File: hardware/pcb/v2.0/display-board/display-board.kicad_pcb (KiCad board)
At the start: 4 copper layers, 92 x 30 mm, 59 parts, among them J1 Conn_01x01_Socket, J2 Conn_01x01_Socket, J3 Conn_01x01_Socket, J4 Conn_01x01_Socket, J5 Conn_01x01_Socket, J6 Conn_01x01_Socket, Q1 AO3400A, Q2 AO3401A, Q3 AO3400A, Q4 AO3401A, Q5 AO3400A, Q6 AO3401A, Q7 AO3400A, SW1 SW_Push, SW2 SW_Push, U1 TLC5940PWP, U2 7Seg 2Dig 0.56in, U3 GS-S2011AB, U4 7Seg 2Dig 0.56in, U5 GS-S2011AB

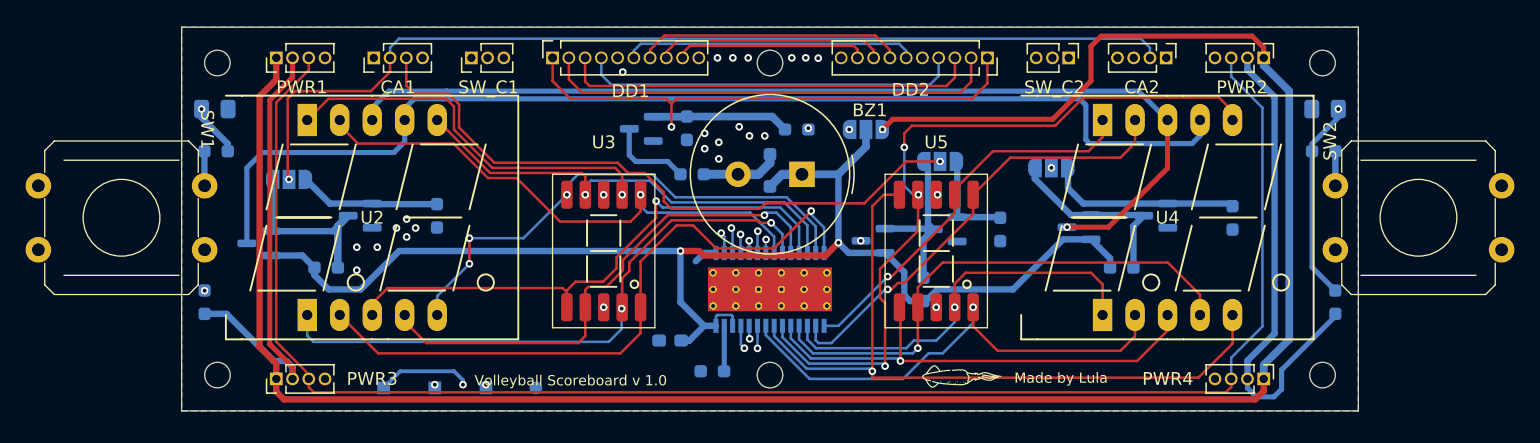
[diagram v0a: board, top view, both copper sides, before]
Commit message: v2.0 of the main and display board is ready and in production
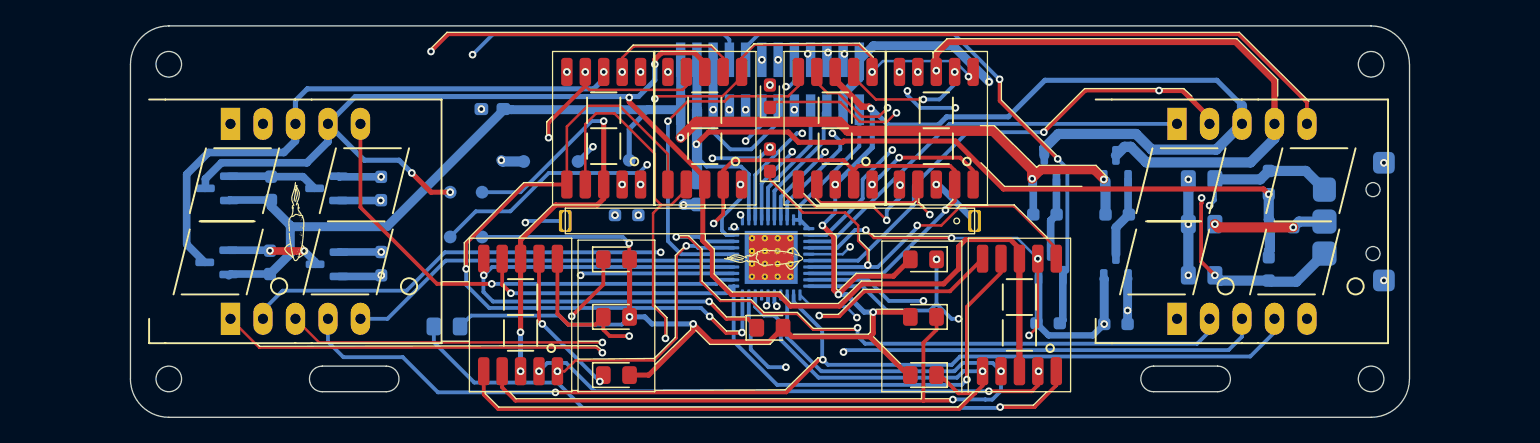
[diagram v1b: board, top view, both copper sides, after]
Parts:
- removed BAT+, CTRL: TestPoint_Pad_1.0x1.0mm, TestPoint:TestPoint_Pad_1.0x1.0mm
- removed BZ1: Buzzer, Buzzer_Beeper:Buzzer_TDK_PS1240P02BT_D12.2mm_H6.5mm
- removed CA1, CA2, PWR1, PWR2, PWR3, PWR4: Conn_01x04_Pin, Connector_PinHeader_1.27mm:PinHeader_1x04_P1.27mm_Vertical
- removed DD1, DD2: Conn_01x10_Pin, Connector_PinSocket_1.27mm:PinSocket_1x10_P1.27mm_Vertical
- removed J1, J2, J3, J4, J5, J6: Conn_01x01_Socket, MountingHole:MountingHole_2mm
- removed the LDO at (73.8, 110.7)
- removed PWRQ1, PWRQ2, PWRQ3, PWR_S1: SolderJumper_3_Open, Jumper:SolderJumper-3_P1.3mm_Open_RoundedPad1.0x1.5mm_NumberLabels
- removed the R10 at (102.1, 90.5)
- removed R13: 1k, Resistor_SMD:R_0603_1608Metric_Pad0.98x0.95mm_HandSolder
- removed the R8 at (93.9, 94.0)
- removed the R9 at (93.5, 90.4)
- removed SW2: SW_Push, Luis:Button_12x12x7.3
- removed SW_C1, SW_C2: Conn_01x03_Pin, Connector_PinHeader_1.27mm:PinHeader_1x03_P1.27mm_Vertical
- removed U1: TLC5940PWP, Package_SO:HTSSOP-28-1EP_4.4x9.7mm_P0.65mm_EP3.4x9.5mm_Mask2.4x6.17mm_ThermalVias
- added 1: TestPoint, TestPoint:TestPoint_Pad_D1.0mm, B.Cu at (77.5, 95.4)
- added 2: TestPoint, TestPoint:TestPoint_Pad_D1.0mm, B.Cu at (75.0, 95.4)
- added 3: TestPoint, TestPoint:TestPoint_Pad_D1.0mm, B.Cu at (77.5, 98.9)
- added 4: TestPoint, TestPoint:TestPoint_Pad_D1.0mm, B.Cu at (75.0, 98.9)
- added A1: Conn_02x12_Odd_Even, Connector_PinHeader_1.27mm:PinHeader_2x12_P1.27mm_Vertical_SMD, B.Cu at (100.0, 87.0)
- added C2: 0.1uF, Capacitor_SMD:C_0603_1608Metric_Pad1.08x0.95mm_HandSolder, B.Cu at (94.3, 95.5)
- added C5: 2.2uF, Capacitor_SMD:C_0805_2012Metric_Pad1.18x1.45mm_HandSolder, B.Cu at (133.7, 94.4)
- added D10: LED, LED_SMD:LED_0603_1608Metric_Pad1.05x0.95mm_HandSolder, F.Cu at (100.0, 87.9)
- added D11: LED, LED_SMD:LED_0603_1608Metric_Pad1.05x0.95mm_HandSolder, F.Cu at (100.0, 92.9)
- added D3: LED, LED_SMD:LED_0805_2012Metric_Pad1.15x1.40mm_HandSolder, F.Cu at (88.0, 100.7)
- added D4: LED, LED_SMD:LED_0805_2012Metric_Pad1.15x1.40mm_HandSolder, F.Cu at (88.0, 105.2)
- added D5: LED, LED_SMD:LED_0805_2012Metric_Pad1.15x1.40mm_HandSolder, F.Cu at (88.0, 109.7)
- added D6: LED, LED_SMD:LED_0805_2012Metric_Pad1.15x1.40mm_HandSolder, F.Cu at (100.0, 106.0)
- added D7: LED, LED_SMD:LED_0805_2012Metric_Pad1.15x1.40mm_HandSolder, F.Cu at (112.0, 100.7)
- added D8: LED, LED_SMD:LED_0805_2012Metric_Pad1.15x1.40mm_HandSolder, F.Cu at (112.0, 105.2)
- added D9: LED, LED_SMD:LED_0805_2012Metric_Pad1.15x1.40mm_HandSolder, F.Cu at (112.0, 109.7)
- added DTEST: LED, LED_SMD:LED_0805_2012Metric_Pad1.15x1.40mm_HandSolder, B.Cu at (74.7, 105.9)
- added G***: LOGO, Luis:lula1, F.Cu at (99.5, 100.6)
- added G***: LOGO, Luis:lula1, F.Cu at (62.9, 97.7)
- added G***: LOGO, Luis:lula1, B.Cu at (140.0, 109.9)
- added H1: MountingHole, MountingHole:MountingHole_2mm, F.Cu at (53.0, 85.4)
- added H2: MountingHole, MountingHole:MountingHole_2mm, F.Cu at (147.0, 85.4)
- added H3: MountingHole, MountingHole:MountingHole_2mm, F.Cu at (53.0, 110.0)
- added H4: MountingHole, MountingHole:MountingHole_2mm, F.Cu at (147.0, 110.0)
- added LDO: TestPoint, TestPoint:TestPoint_Pad_D1.0mm, B.Cu at (85.0, 93.0)
- added Q8: AO3401A, Package_TO_SOT_SMD:SOT-23, B.Cu at (127.0, 93.5)
- added R1: 651, Resistor_SMD:R_0603_1608Metric_Pad0.98x0.95mm_HandSolder, B.Cu at (88.8, 97.2)
- added R12: 10K, Resistor_SMD:R_0603_1608Metric_Pad0.98x0.95mm_HandSolder, B.Cu at (127.1, 97.2)
- added TCL5951: TLC5951RHA, Package_DFN_QFN:Texas_RHA0040B_VQFN-40-1EP_6x6mm_P0.5mm_EP4.15x4.15mm_ThermalVias, B.Cu at (100.1, 100.5)
- added U2: GS-S2011AB, Luis:GS-2011AB, F.Cu at (87.0, 90.4)
- added U5: GS-S2011AB, Luis:GS-2011AB, F.Cu at (94.9, 90.4)
- added U7: GS-S2011AB, Luis:GS-2011AB, F.Cu at (105.1, 90.4)
- added U9: GS-S2011AB, Luis:GS-2011AB, F.Cu at (113.0, 90.4)
- added VCC: TestPoint, TestPoint:TestPoint_Pad_D1.0mm, B.Cu at (89.0, 92.9)
- C1: value C -> 10uF
- C3: renamed from C2; value 0.1uF -> 2.2uF
- C4: renamed from C3; value 0.1uF -> 2.2uF
- D1: value D -> LED; footprint Diode_SMD:D_SOD-323_HandSoldering -> Luis:LED Bar; moved to F.Cu
- G***: moved to B.Cu
- GND: value TestPoint_Pad_D1.0mm -> TestPoint
- R11: value 1k -> 10K
- R4: value 651 -> 100k
- SW1: value SW_Push -> ~; footprint Luis:Button_12x12x7.3 -> Luis:Thumbwheel; moved to B.Cu
- moved SW1 97.8 mm to (147.1, 97.7), turned to 90 degrees
- moved R3 84.4 mm to (140.0, 98.2), turned to 0 degrees
- moved C4 77.7 mm to (133.7, 97.9), turned to 180 degrees
- moved Q4 67.4 mm to (56.8, 95.1)
- moved R8 66.8 mm to (61.0, 95.1), turned to 90 degrees
- moved R7 66.6 mm to (69.6, 95.1)
- moved Q3 64.9 mm to (65.3, 95.1)
- moved G*** 55.0 mm to (60.0, 109.9)
- moved R4 45.9 mm to (139.0, 94.7), turned to 90 degrees
- moved Q7 38.6 mm to (127.0, 101.2), turned to 90 degrees
- moved C1 22.8 mm to (78.3, 88.9)
- moved G*** 21.7 mm to (60.2, 85.4)
- moved R11 21.1 mm to (127.0, 105.7)
- moved GND 17.7 mm to (80.7, 93.0)
- moved C3 16.2 mm to (133.7, 101.9)
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- renumbered R7 to R10, R12 to R2, R14 to R3, R1 to R5, R2 to R6, R3 to R7, R5 to R8, R6 to R9, U2 to U3, U3 to U4, U5 to U6, U4 to U8
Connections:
- net Net-(PWRQ1-A) renamed /MUX_1
- net Net-(PWRQ2-A) renamed /MUX_2
- net Net-(PWRQ3-A) renamed /MUX_3
- C1 pad 1: VCC -> /VCC_CTRL
- C3 pad 1: /SW2 -> /SW_1
- C4 pad 1: /SW1 -> /SW_2
- D1 pad 1: VCC -> /OUTB2
- D1 pad 2: Net-(BZ1-+) -> /7SEG_MUX_4
- Q2 pad 2: VCC -> /VCC_CTRL
- Q2 pad 3: /7SEG_DD_2 -> /7SEG_MUX_1
- Q4 pad 2: VCC -> /VCC_CTRL
- Q4 pad 3: /7SEG_DD_1 -> /7SEG_MUX_2
- Q6 pad 2: VCC -> /VCC_CTRL
- Q6 pad 3: /7SEG_SD -> /7SEG_MUX_3
- Q7 pad 1: Net-(Q7-G) -> /MUX_4
- R10 pad 1: VCC -> /VCC_CTRL
- R11 pad 1: Net-(R11-Pad1) -> /MUX_4
- R11 pad 2: /SW2 -> GND
- R2 pad 1: /LDO -> /LDO_CTRL
- R2 pad 2: /SW2 -> /SW_1
- R3 pad 1: /LDO -> /LDO_CTRL
- R3 pad 2: /SW1 -> /SW_2
- R4 pad 1: Net-(U1-IREF) -> /LDO_CTRL
- R4 pad 2: GND -> /SW_3
- R6 pad 1: VCC -> /VCC_CTRL
- R8 pad 1: VCC -> /VCC_CTRL
- SW1 pad 1: Net-(R13-Pad1) -> /SW_1
- SW1 pad 2: GND -> /SW_3
- U3 pad 1: Net-(U1-OUT2) -> /OUTR2
- U3 pad 10: Net-(U1-OUT0) -> /OUTR0
- U3 pad 2: Net-(U1-OUT7) -> /OUTR7
- U3 pad 3: Net-(U1-OUT4) -> /OUTR4
- U3 pad 4: Net-(U1-OUT3) -> /OUTR3
- U3 pad 5: Net-(U1-OUT6) -> /OUTR6
- U3 pad 6: Net-(U1-OUT5) -> /OUTR5
- U3 pad 7: /7SEG_DD_2 -> /7SEG_MUX_2
- U3 pad 8: /7SEG_DD_1 -> /7SEG_MUX_1
- U3 pad 9: Net-(U1-OUT1) -> /OUTR1
- U4 pad 1: Net-(U1-OUT4) -> /OUTB4
- U4 pad 10: Net-(U1-OUT6) -> /OUTB6
- U4 pad 2: Net-(U1-OUT3) -> /OUTB3
- U4 pad 3: /7SEG_SD -> /7SEG_MUX_1
- U4 pad 4: Net-(U1-OUT2) -> /OUTB2
- U4 pad 5: Net-(U1-OUT7) -> /OUTB7
- U4 pad 6: Net-(U1-OUT1) -> /OUTB1
- U4 pad 7: Net-(U1-OUT0) -> /OUTB0
- U4 pad 8: /7SEG_SD -> /7SEG_MUX_1
- U4 pad 9: Net-(U1-OUT5) -> /OUTB5
- U6 pad 1: Net-(U1-OUT12) -> /OUTB4
- U6 pad 10: Net-(U1-OUT14) -> /OUTB6
- U6 pad 2: Net-(U1-OUT11) -> /OUTB3
- U6 pad 3: /7SEG_SD -> /7SEG_MUX_2
- U6 pad 4: Net-(U1-OUT10) -> /OUTB2
- U6 pad 5: Net-(U1-OUT15) -> /OUTB7
- U6 pad 6: Net-(U1-OUT9) -> /OUTB1
- U6 pad 7: Net-(U1-OUT8) -> /OUTB0
- U6 pad 8: /7SEG_SD -> /7SEG_MUX_2
- U6 pad 9: Net-(U1-OUT13) -> /OUTB5
- U8 pad 1: Net-(U1-OUT10) -> /OUTR2
- U8 pad 10: Net-(U1-OUT8) -> /OUTR0
- U8 pad 2: Net-(U1-OUT15) -> /OUTR7
- U8 pad 3: Net-(U1-OUT12) -> /OUTR4
- U8 pad 4: Net-(U1-OUT11) -> /OUTR3
- U8 pad 5: Net-(U1-OUT14) -> /OUTR6
- U8 pad 6: Net-(U1-OUT13) -> /OUTR5
- U8 pad 7: /7SEG_DD_2 -> /7SEG_MUX_4
- U8 pad 8: /7SEG_DD_1 -> /7SEG_MUX_3
- U8 pad 9: Net-(U1-OUT9) -> /OUTR1
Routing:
- net /LDO: track 198.6 -> 0.00 mm, vias 2 -> 0
- net /BAT+: track 186.5 -> 0.00 mm, vias 2 -> 0
- net /BUZZER: track 164.1 -> 0.00 mm, vias 1 -> 0
- net /7SEG_MUX_3: track 0.00 -> 150.7 mm, vias 0 -> 8
- net /OUTR5: track 0.00 -> 119.2 mm, vias 0 -> 2
- net /OUTR1: track 0.00 -> 116.3 mm, vias 0 -> 2
- net /OUTR0: track 0.00 -> 115.5 mm
- net /7SEG_MUX_2: track 0.00 -> 113.2 mm, vias 0 -> 4
- net /OUTR6: track 0.00 -> 111.5 mm
- net /7SEG_MUX_4: track 0.00 -> 109.9 mm, vias 0 -> 6
- net VCC: track 103.9 -> 0.00 mm, vias 2 -> 0
- net /VCC_CTRL: track 0.00 -> 100.5 mm, vias 0 -> 3
- net /OUTB0: track 0.00 -> 95.3 mm, vias 0 -> 7
- net /SW1: track 94.8 -> 0.00 mm, vias 2 -> 0
- net /SW2: track 90.6 -> 0.00 mm, vias 1 -> 0
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- added copper zone on In1.Cu, net GND
- removed copper zone on B.Cu, net GND
- removed copper zone on F.Cu, net GND
- removed copper zone on In2.Cu, net GND
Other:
- board size 92 x 30 mm -> 100 x 30.6 mm
- board text added: "1"
- board text added: "2"
- board text added: "3"
- board text added: "4"
- board text added: "A"
- board text added: "Button Decoupling"
- board text added: "Display Board V2.0"
- board text added: "G"
- board text added: "GND"
- board text added: "LDO"
- board text added: "MUX"
- board text added: "MUX 1"
- board text added: "MUX 2"
- board text added: "MUX 3"
- board text added: "MUX 4"
- board text added: "Os Doze"
- board text added: "SW"
- board text added: "VCC"
- board text added: "blank"
- board text added: "gsclk"
- board text added: "sc"
- board text added: "si"
- board text added: "so"
- board text added: "xl"
- board text removed: "Volleyball Scoreboard v 1.0"

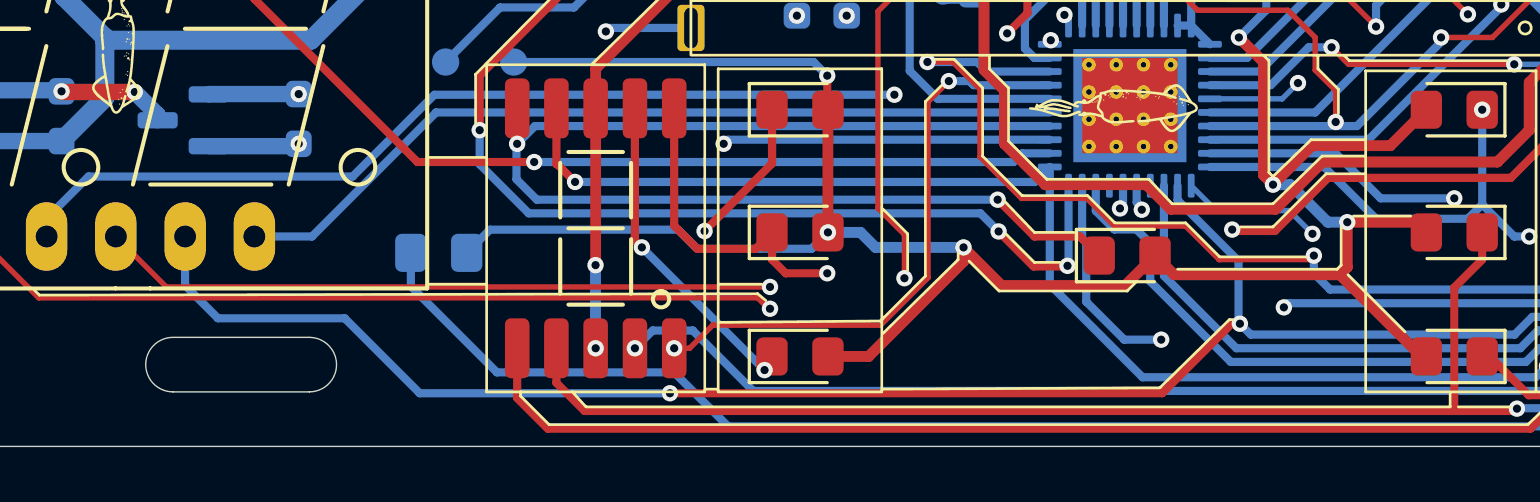
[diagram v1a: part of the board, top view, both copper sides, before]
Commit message: new version in the works, time is not yet functional but the new board is very much working
ds3231 vbat is switched with the vcc - fixed
have to fix capacitor resonance since it is really annoying
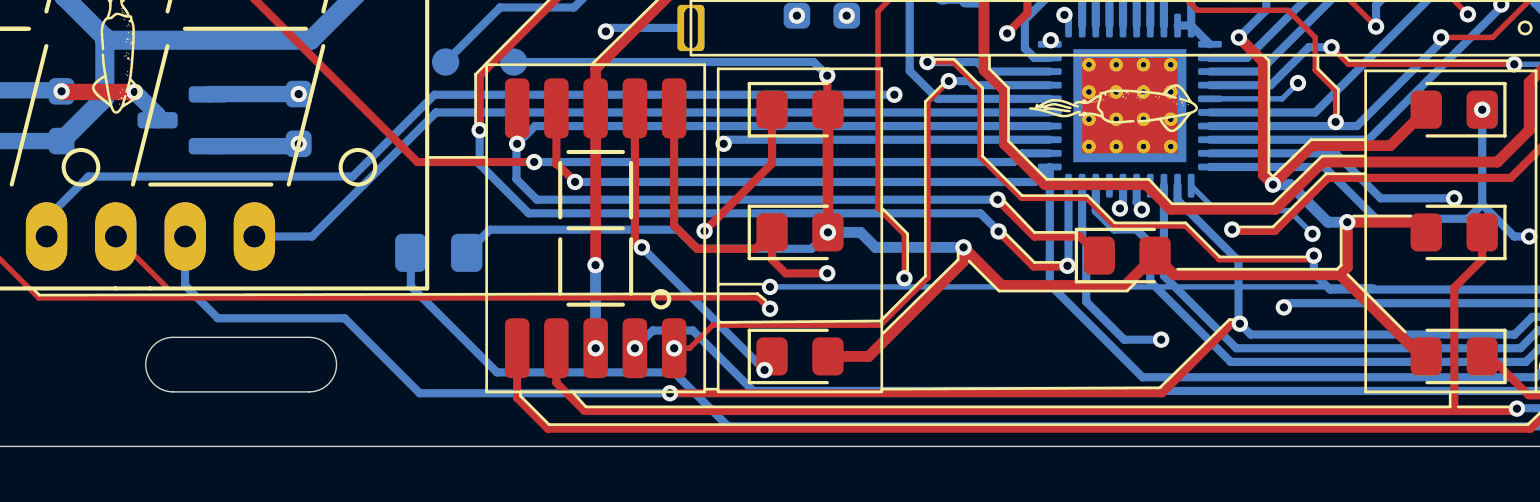
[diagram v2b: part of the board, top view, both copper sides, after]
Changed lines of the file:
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@@
 	)
 	(gr_line
-		(start 74.32 107.05)
-		(end 76.445 107.05)
-		(stroke
-			(width 0.1)
-			(type default)
-		)
-		(layer "F.SilkS")
-	)
-	(gr_line
 		(start 111.245 96.3)
 		(end 111.445 96.1)
@@
 	)
 	(gr_line
+		(start 74.32 107.05)
+		(end 72.195 107.05)
+		(stroke
+			(width 0.1)
+			(type default)
+		)
+		(layer "B.SilkS")
+	)
+	(gr_line
 		(start 142.995 91.9)
 		(end 131.995 91.9)
@@
 		(net 33)
 	)
-	(segment
-		(start 86.895 107.15)
-		(end 64.75 107.15)
-		(width 0.2)
-		(layer "F.Cu")
-		(net 33)
-	)
 	(via
 		(at 101.245 109.08462)
@@
 		(layer "B.Cu")
 		(net 33)
+	)
+	(segment
+		(start 86.895 107.15)
+		(end 109.04 107.15)
+		(width 0.2)
+		(layer "B.Cu")
+		(net 33)
